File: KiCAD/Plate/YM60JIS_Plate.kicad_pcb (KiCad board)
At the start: 2 copper layers, 285.1 x 94.6 mm, 69 parts, among them SW1 SW_Push, SW10 SW_Push, SW11 SW_Push, SW12 SW_Push, SW13 SW_Push, SW14 SW_Push, SW15 SW_Push, SW16 SW_Push, SW17 SW_Push, SW18 SW_Push, SW19 SW_Push, SW2 SW_Push, SW20 SW_Push, SW21 SW_Push, SW22 SW_Push, SW23 SW_Push, SW24 SW_Push, SW25 SW_Push, SW26 SW_Push, SW27 SW_Push, SW28 SW_Push, SW29 Space, SW3 SW_Push, SW30 SW_Push, SW31 SW_Push, SW32 SW_Push, SW33 SW_Push, SW34 SW_Push, SW35 SW_Push, SW36 SW_Push, SW37 SW_Push, SW38 SW_Push, SW39 SW_Push, SW4 SW_Push, SW40 SW_Push, SW41 SW_Push, SW42 SW_Push, SW43 SW_Push, SW44 SW_Push, SW45 SW_Push, SW46 SW_Push, SW47 SW_Push, SW48 SW_Push, SW49 SW_Push, SW5 SW_Push, SW50 SW_Push, SW51 SW_Push, SW52 SW_Push, SW53 SW_Push, SW54 SW_Push, SW55 SW_Push, SW56 SW_Push, SW57 SW_Push, SW58 SW_Push, SW59 SW_Push, SW6 SW_Push, SW60 SW_Push, SW61 SW_Push, SW62 SW_Push, SW63 Yen, SW64 Backspace, SW65 ISOEnter, SW66 SW_Push, SW67 SW_Push, SW7 SW_Push, SW8 SW_Push, SW9 SW_Push

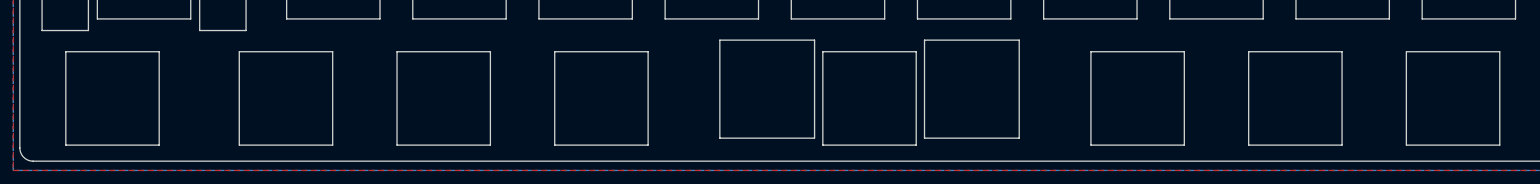
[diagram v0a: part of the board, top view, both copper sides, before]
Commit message: Rework PCB and plate for the HHKB-style bottom row (v1.1.2)
- Schematic: switch footprints for the former 1.25u/1.5u bottom-row keys
  are now 1u.
- PCB: move all bottom-row switches and diodes to the new 2.5u-spacebar
  layout, add SW68/D68 (COL4) and SW69/D69 (COL7), replace the 2.75u/3u
  spacebar stabilizers with a 2u stabilizer, and reroute row 4. Move a
  GND via off the new stabilizer hole and the text logo off the かな
  switch. DRC: 0 unconnected pads, no new errors vs v1.1.1.
- Plate: switch and stabilizer cutouts for the new bottom row.
- Version label: "YM60JIS Trilingual v1.1.2 @ymkn & @themrsung".
- PCB and plate are now saved in KiCAD 10 format.
- Add before/after 3D render comparison page (doc/pcb-compare).

Co-Authored-By: Claude Opus 5.5 (1M context) <noreply@anthropic.com>
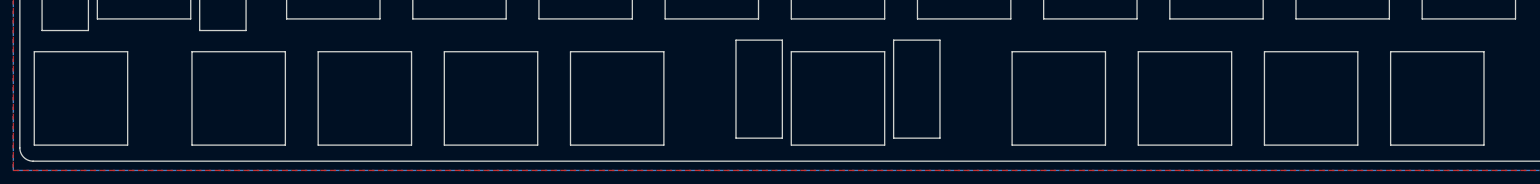
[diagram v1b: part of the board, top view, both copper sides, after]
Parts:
- added SW68: SW_Push, kbd_SW_Hole:SW_Hole_1u, F.Cu at (185.7, 133.3)
- added SW69: SW_Push, kbd_SW_Hole:SW_Hole_1u, F.Cu at (252.4, 133.3)
- SW10, SW15, SW20, SW42, SW47, SW52: footprint kbd_SW_Hole:SW_Hole_1.25u -> kbd_SW_Hole:SW_Hole_1u
- SW29: value Space -> SW_Push; footprint kbd_SW_Hole:SW_Hole_2u3u_JLC -> kbd_SW_Hole:SW_Hole_2u
- SW5: footprint kbd_SW_Hole:SW_Hole_1.5u -> kbd_SW_Hole:SW_Hole_1u
- moved SW20 16.7 mm to (166.7, 133.3)
- moved SW15 11.9 mm to (147.6, 133.3)
- moved SW10 7.14 mm to (128.6, 133.3)
- moved SW42 7.14 mm to (271.5, 133.3)
- moved SW29 4.76 mm to (219.1, 133.3)
- moved SW5 4.76 mm to (104.8, 133.3)
- moved SW52 2.38 mm to (309.6, 133.3)
- moved SW47 2.38 mm to (290.5, 133.3)
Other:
- board text added: "YM60JIS Trilingual v1.1.2 @ymkn & @themrsung"
- board text removed: "YM60JIS v1.1 @ymkn"
